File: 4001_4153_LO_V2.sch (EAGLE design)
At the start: 107 parts, among them IC1 ADF4153BRUZ-RL7, IC10 ATTINY45V-10SU, IC11 LD117ASTR, IC2 7809DT, IC4 ADF4001BRUZ, IC5 74LVC2G17GV,125, IC6 74LVC2G17GV,125, IC7 74LVC2G17GV,125, IC8 ADT1-1WT-1+, IC9 7805DT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

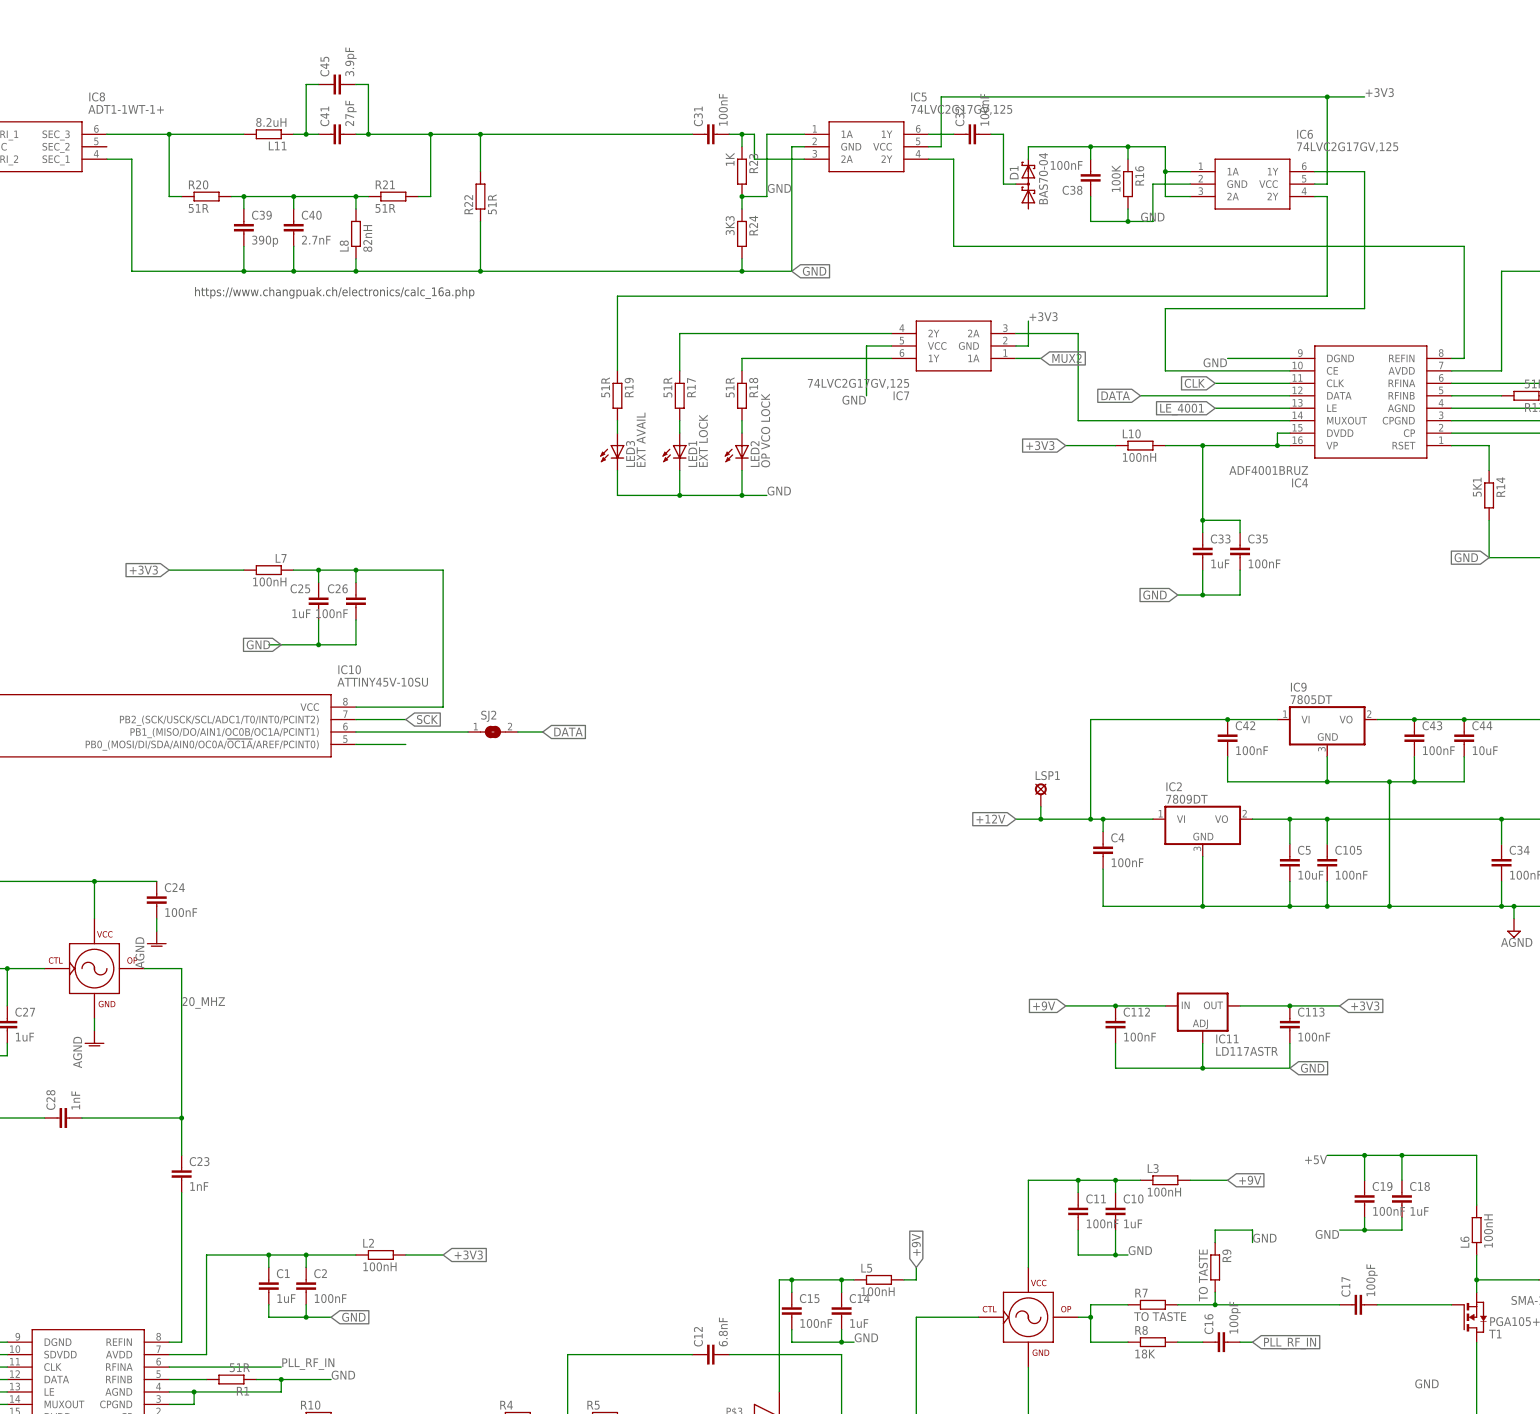
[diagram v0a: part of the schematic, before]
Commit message: Size change and pre-release tweaks
Updated sizes, sorted out component name positions on PCB, added 10R to PGA105+drive  ref Andy JNT
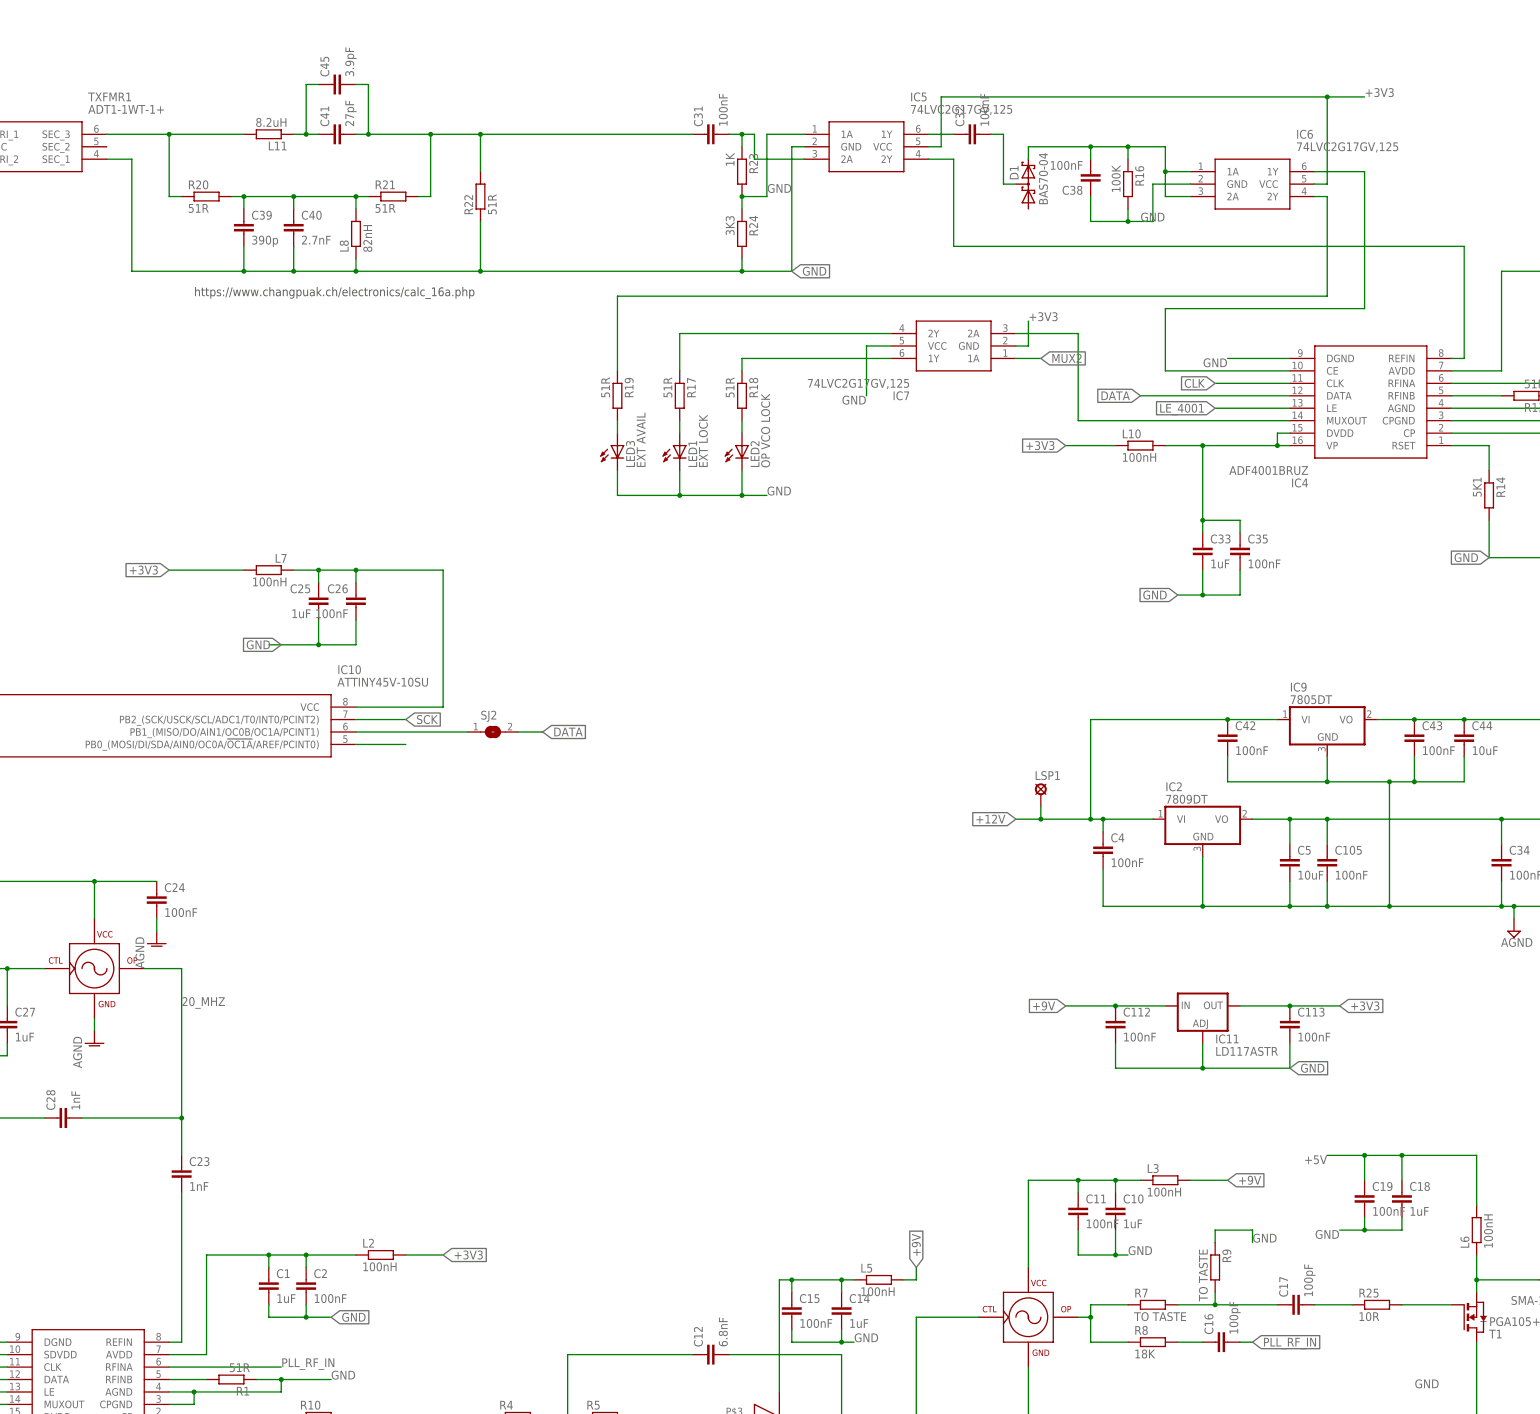
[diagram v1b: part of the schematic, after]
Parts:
- added R25: 10R, rcl:R-EU_R0603
- renumbered IC8 to TXFMR1
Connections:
- new net N$21: C17.2, R25.1
- net N$11: now also R25.2; no longer C17.2
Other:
- moved on the sheet: C17
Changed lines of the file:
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@@
 <part name="R19" library="rcl" deviceset="R-EU_" device="R0603" value="51R"/>
 <part name="LED3" library="led" deviceset="LED" device="3MM" value="EXT AVAIL"/>
-<part name="IC8" library="ADT1-1WT-1+" deviceset="ADT1-1WT-1+" device=""/>
+<part name="TXFMR1" library="ADT1-1WT-1+" deviceset="ADT1-1WT-1+" device=""/>
 <part name="R20" library="rcl" deviceset="R-EU_" device="R0603" value="51R"/>
 <part name="C39" library="resistor" deviceset="C-EU" device="C0603" value="390p"/>
@@
 <part name="C44" library="rcl" deviceset="C-EU" device="C0805" value="10uF"/>
 <part name="LSP1" library="solpad" deviceset="LSP13" device=""/>
+<part name="R25" library="rcl" deviceset="R-EU_" device="R0603" value="10R"/>
 </parts>
 <sheets>
@@
 <instance part="C16" gate="G$1" x="403.86" y="99.06" rot="R90"/>
 <instance part="T1" gate="G$1" x="457.2" y="104.14" rot="MR180"/>
-<instance part="C17" gate="G$1" x="431.8" y="106.68" rot="R90"/>
+<instance part="C17" gate="G$1" x="419.1" y="106.68" rot="R90"/>
 <instance part="C18" gate="G$1" x="441.96" y="129.54"/>
 <instance part="C19" gate="G$1" x="434.34" y="129.54"/>
@@
 <instance part="R19" gate="G$1" x="281.94" y="292.1" rot="R270"/>
 <instance part="LED3" gate="G$1" x="281.94" y="281.94"/>
-<instance part="IC8" gate="G$1" x="147.32" y="345.44"/>
+<instance part="TXFMR1" gate="G$1" x="147.32" y="345.44"/>
 <instance part="R20" gate="G$1" x="198.12" y="332.74"/>
 <instance part="C39" gate="G$1" x="205.74" y="327.66"/>
@@
 <instance part="C44" gate="G$1" x="454.66" y="223.52"/>
 <instance part="LSP1" gate="1" x="368.3" y="210.82"/>
+<instance part="R25" gate="G$1" x="436.88" y="106.68"/>
 </instances>
 <busses>
@@
 <wire x1="215.9" y1="322.58" x2="215.9" y2="317.5" width="0.1524" layer="91"/>
 <junction x="215.9" y="317.5"/>
-<pinref part="IC8" gate="G$1" pin="SEC_1"/>
+<pinref part="TXFMR1" gate="G$1" pin="SEC_1"/>
 <wire x1="177.8" y1="340.36" x2="182.88" y2="340.36" width="0.1524" layer="91"/>
 <wire x1="205.74" y1="317.5" x2="182.88" y2="317.5" width="0.1524" layer="91"/>
@@
 </segment>
 <segment>
-<pinref part="IC8" gate="G$1" pin="PRI_2"/>
+<pinref part="TXFMR1" gate="G$1" pin="PRI_2"/>
 <wire x1="147.32" y1="340.36" x2="139.7" y2="340.36" width="0.1524" layer="91"/>
 <wire x1="129.54" y1="342.9" x2="139.7" y2="342.9" width="0.1524" layer="91"/>
@@
 <net name="N$11" class="0">
 <segment>
-<wire x1="436.88" y1="106.68" x2="452.12" y2="106.68" width="0.1524" layer="91"/>
 <pinref part="T1" gate="G$1" pin="G"/>
-<pinref part="C17" gate="G$1" pin="2"/>
+<pinref part="R25" gate="G$1" pin="2"/>
+<wire x1="441.96" y1="106.68" x2="452.12" y2="106.68" width="0.1524" layer="91"/>
 </segment>
 </net>
@@
 <pinref part="R7" gate="G$1" pin="2"/>
 <wire x1="396.24" y1="106.68" x2="403.86" y2="106.68" width="0.1524" layer="91"/>
-<wire x1="403.86" y1="106.68" x2="429.26" y2="106.68" width="0.1524" layer="91"/>
+<wire x1="403.86" y1="106.68" x2="416.56" y2="106.68" width="0.1524" layer="91"/>
 <pinref part="C17" gate="G$1" pin="1"/>
 <pinref part="R9" gate="G$1" pin="2"/>
@@
 <net name="N$34" class="0">
 <segment>
-<pinref part="IC8" gate="G$1" pin="PRI_1"/>
+<pinref part="TXFMR1" gate="G$1" pin="PRI_1"/>
 <wire x1="129.54" y1="345.44" x2="147.32" y2="345.44" width="0.1524" layer="91"/>
 <pinref part="X9" gate="G1" pin="1"/>
@@
 <net name="N$33" class="0">
 <segment>
-<pinref part="IC8" gate="G$1" pin="SEC_3"/>
+<pinref part="TXFMR1" gate="G$1" pin="SEC_3"/>
 <pinref part="L11" gate="G$1" pin="2"/>
 <wire x1="177.8" y1="345.44" x2="190.5" y2="345.44" width="0.1524" layer="91"/>
@@
 </segment>
 </net>
+<net name="N$21" class="0">
+<segment>
+<pinref part="R25" gate="G$1" pin="1"/>
+<wire x1="424.18" y1="106.68" x2="431.8" y2="106.68" width="0.1524" layer="91"/>
+<pinref part="C17" gate="G$1" pin="2"/>
+</segment>
+</net>
